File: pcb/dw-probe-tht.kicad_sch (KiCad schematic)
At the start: 26 parts, among them Q1 IRLML6402, Q2 IRLML6402, SW1 SW_Push, U1 LM1117T-3.3

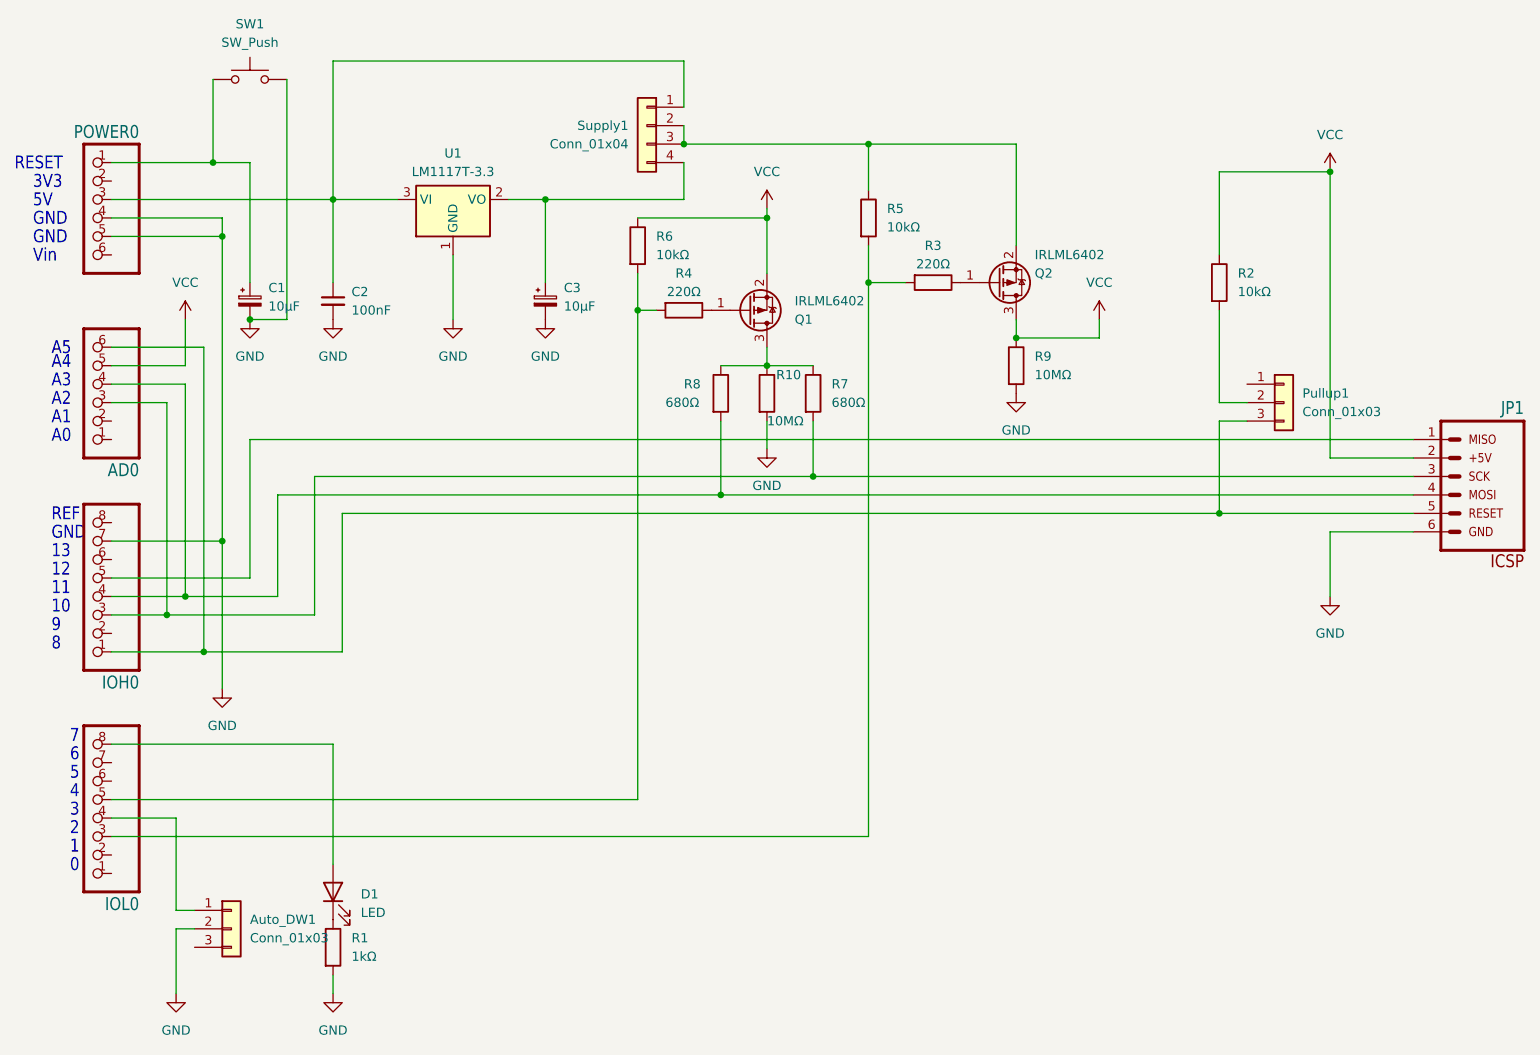
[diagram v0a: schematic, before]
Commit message: new dw-link probe V3.1
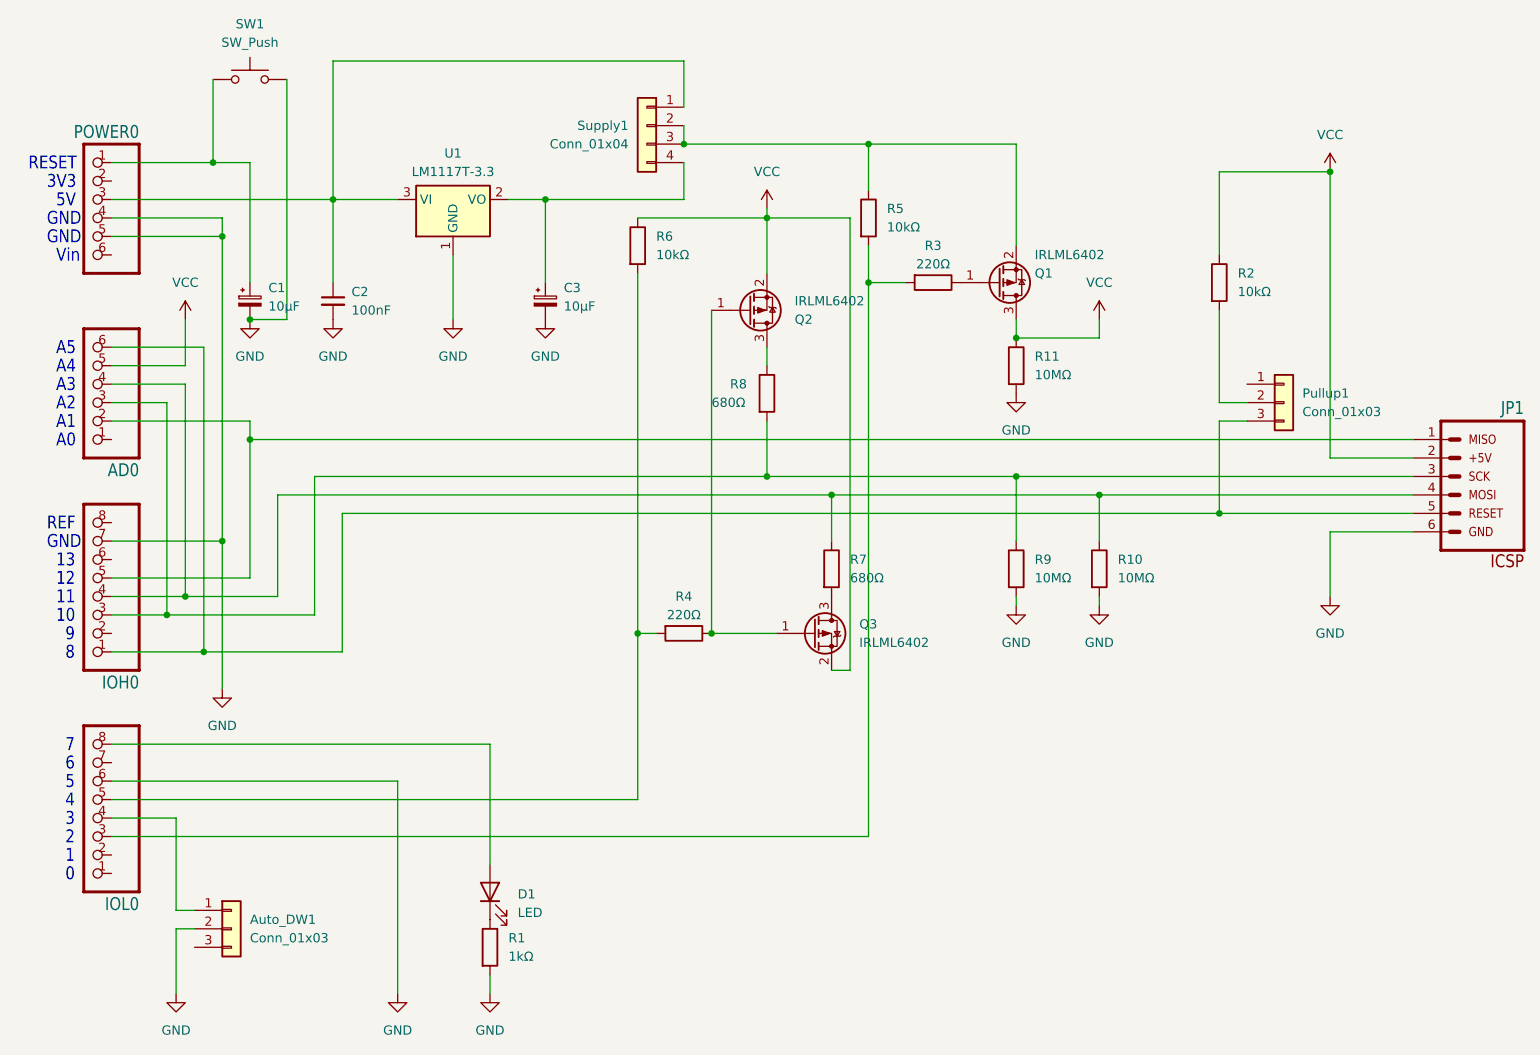
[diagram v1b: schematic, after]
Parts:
- added Q3: IRLML6402, Package_TO_SOT_SMD:SOT-23_Handsoldering, symbol Transistor_FET:IRLML6402
- added R9: 10MΩ, Resistor_THT:R_Axial_DIN0207_L6.3mm_D2.5mm_P7.62mm_Horizontal, symbol Device:R
- renumbered Q2 to Q1, Q1 to Q2, R9 to R11
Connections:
- net GND: now also IOL0.6, R9.2
- net VCC: now also Q3.2 (S)
- net at Q2.1 (G), R4.1: now also Q3.1 (G)
- net at R10.1, R7.1: now also AD0.4, IOH0.4, JP1.4; no longer Q2.3 (D), R8.1
- net at AD0.3, IOH0.3, JP1.3: now also R8.2, R9.1; no longer R7.2
- net at IOH0.5, JP1.1: now also AD0.2
- new net: Q3.3 (D), R7.2
- new net: Q2.3 (D), R8.1
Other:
- title: dw-link probe (THT) -> dw-link probe (THT) V3.1
- moved on the sheet: D1, R1, R4, R7, R8
